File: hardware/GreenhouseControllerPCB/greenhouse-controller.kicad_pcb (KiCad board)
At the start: 2 copper layers, 208 x 132 mm, 72 parts, among them J1 Motor 2, J10 ALARM contact, J11 AC-Mains, J12 DM1AA-SF-PEJ72, J13 MODBUS RS485 S200, J2 24V in, J3 I2C Display, J4 Keypad, J6 Motor 3, J7 Motor 1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

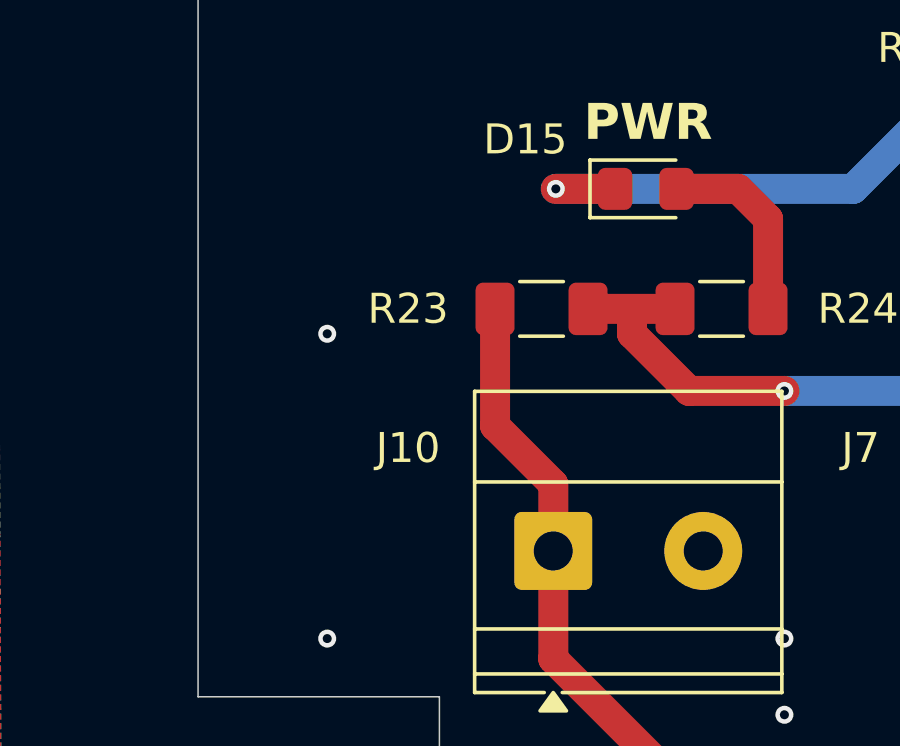
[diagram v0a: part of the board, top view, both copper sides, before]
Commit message: rc.1.5.5 — IO MUX pin glitch filter on GPIO42 (motor-alarm EMI defense)
Software complement to the 1.8 kΩ shunt resistor installed on unit
5C88 (2026-05-29) across the alarm input pad. The shunt sets a
current-amplitude floor that EMI must overcome to flip the GPIO
through threshold (lowering source impedance from 1 kΩ to ~643 Ω);
this filter sets a duration floor at the IO MUX (~25 ns) before any
interrupt is raised.

ESP-IDF's gpio_new_pin_glitch_filter() inserts a 2-IO-MUX-clock-cycle
filter into the input path between the pad and the GPIO matrix
interrupt logic. Sub-25 ns pulses — the bulk of capacitively-coupled
EMI on long unterminated cables — are dropped at silicon, costing
zero CPU cycles. Genuine mechanical alarm-contact transitions settle
in ≥ 1 ms so they pass through unaffected.

The four-layer defense stack now in place on the alarm pipeline:

  hardware divider  → amplitude floor (~mA injection required)   [HW]
  pin glitch filter → duration floor (≥ 25 ns to register)       [rc.1.5.5]
  ISR rate-limit    → ≥ 5 ms between accepted edges              [rc.1.5.3]
  task debounce     → re-read live pin 75 ms after edge          [rc.1.4 baseline]

For an EMI event to now produce a spurious alarm it must clear all
four floors simultaneously. Real alarm transitions clear them by
construction.

Failure to create the filter is non-fatal — the rate-limit + task
debounce remain in place, just less robustly; a warning is logged
and operation continues. On success: ESP_LOGI emits
"GPIO42 pin glitch filter enabled (~25 ns IO MUX drop)" at boot.

Build + OTA verified on unit 5C88 (192.168.20.150):
  fw_ver         = 2.0.0-rc.1.5.5
  asset_version  = 2.0.0-rc.1.5.5
  bank=A accepted=true (past T1's 30 s healthy mark)
  no rollback, no coredump

Flash: 64.7 % → 64.8 % (+1504 B — IDF gpio_filter component).
RAM:   18.9 % unchanged (+8 B handle pointer in .bss).

Added pull down resistor to PCB for alarm input tom meet 3,3V compliance of GPIO and mitigate EMI on input.
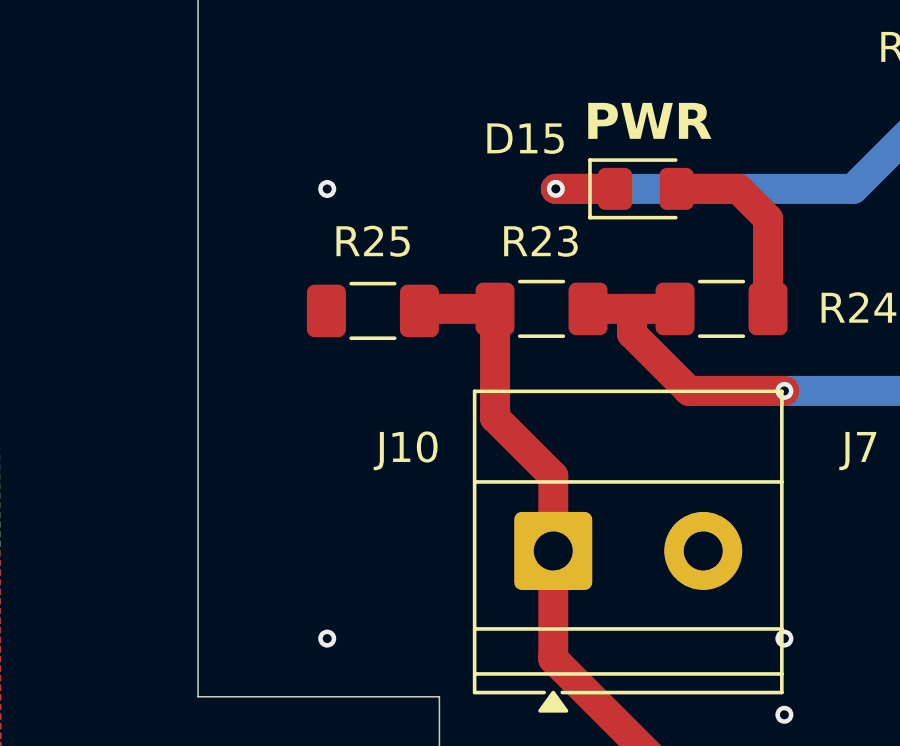
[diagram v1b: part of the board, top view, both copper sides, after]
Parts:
- added R25: 1K8, Resistor_SMD:R_1206_3216Metric_Pad1.30x1.75mm_HandSolder, F.Cu at (49.8, 126.2)
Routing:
- net /OPTO_INPUT: track 213.4 -> 216.0 mm
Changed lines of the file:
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@@
 	(title_block
 		(title "PCB Kas-controller Wenumseveld")
-		(date "2026-05-01")
+		(date "2026-05-29")
 		(rev "Remko Welling")
 		(company "RFSee")
 		(comment 1 "remko@rfsee.nl")
 		(comment 2 "https://www.rfsee.nl")
-		(comment 3 "V 1.1.0")
+		(comment 3 "V 1.1.1")
 	)
 	(layers
@@
 		)
 	)
+	(footprint "Resistor_SMD:R_1206_3216Metric_Pad1.30x1.75mm_HandSolder"
+		(layer "F.Cu")
+		(at 49.784 126.238 180)
+		(descr "Resistor SMD 1206 (3216 Metric), square (rectangular) end terminal, IPC-7351 nominal with elongated pad for handsoldering. (Body size source: IPC-SM-782 page 72, https://www.pcb-3d.com/wordpress/wp-content/uploads/ipc-sm-782a_amendment_1_and_2.pdf)")
+		(tags "resistor handsolder")
+		(property "Reference" "R25"
+			(at 0 2.286 0)
+			(layer "F.SilkS")
+			(effects
+				(font
+					(size 1 1)
+					(thickness 0.15)
+				)
+			)
+		)
+		(property "Value" "1K8"
+			(at 0 1.83 0)
+			(layer "F.Fab")
+			(effects
+				(font
+					(size 1 1)
+					(thickness 0.15)
+				)
+			)
+		)
+		(property "Datasheet" ""
+			(at 0 0 0)
+			(layer "F.Fab")
+			(hide yes)
+			(effects
+				(font
+					(size 1.27 1.27)
+				)
+			)
+		)
+		(property "Description" "Resistor"
+			(at 0 0 0)
+			(layer "F.Fab")
+			(hide yes)
+			(effects
+				(font
+					(size 1.27 1.27)
+				)
+			)
+		)
+		(property ki_fp_filters "R_*")
+		(sheetname "/")
+		(sheetfile "greenhouse-controller.kicad_sch")
+		(units
+			(unit
+				(name "A")
+				(pins "1" "2")
+			)
+		)
+		(attr smd)
+		(duplicate_pad_numbers_are_jumpers no)
+		(fp_line
+			(start -0.727064 0.91)
+			(end 0.727064 0.91)
+			(stroke
+				(width 0.12)
+				(type solid)
+			)
+			(layer "F.SilkS")
+		)
+		(fp_line
+			(start -0.727064 -0.91)
+			(end 0.727064 -0.91)
+			(stroke
+				(width 0.12)
+				(type solid)
+			)
+			(layer "F.SilkS")
+		)
+		(fp_rect
+			(start -2.45 -1.13)
+			(end 2.45 1.13)
+			(stroke
+				(width 0.05)
+				(type solid)
+			)
+			(fill no)
+			(layer "F.CrtYd")
+		)
+		(fp_rect
+			(start -1.6 -0.8)
+			(end 1.6 0.8)
+			(stroke
+				(width 0.1)
+				(type solid)
+			)
+			(fill no)
+			(layer "F.Fab")
+		)
+		(fp_text user "${REFERENCE}"
+			(at 0 0 0)
+			(layer "F.Fab")
+			(effects
+				(font
+					(size 0.8 0.8)
+					(thickness 0.12)
+				)
+			)
+		)
+		(pad "1" smd roundrect
+			(at -1.55 0 180)
+			(size 1.3 1.75)
+			(layers "F.Cu" "F.Mask" "F.Paste")
+			(roundrect_rratio 0.192308)
+			(net "/OPTO_INPUT")
+			(pintype "passive")
+		)
+		(pad "2" smd roundrect
+			(at 1.55 0 180)
+			(size 1.3 1.75)
+			(layers "F.Cu" "F.Mask" "F.Paste")
+			(roundrect_rratio 0.192308)
+			(net "/GND")
+			(pintype "passive")
+		)
+		(embedded_fonts no)
+		(model "${KICAD10_3DMODEL_DIR}/Resistor_SMD.3dshapes/R_1206_3216Metric.step"
+			(offset
+				(xyz 0 0 0)
+			)
+			(scale
+				(xyz 1 1 1)
+			)
+			(rotate
+				(xyz 0 0 0)
+			)
+		)
+	)
 	(footprint "my-KiCad-library:SRD-05VDC-SL-C"
 		(layer "F.Cu")
@@
 		(tags "resistor handsolder")
 		(property "Reference" "R23"
-			(at 4.45 0 0)
+			(at 0.033 2.218 0)
 			(layer "F.SilkS")
 			(effects
@@
 	)
 	(via
-		(at 48.26 127)
+		(at 48.26 122.174)
 		(size 0.6)
 		(drill 0.3)
@@
 	)
 	(segment
-		(start 151.13 111.252)
-		(end 163.83 111.252)
+		(start 51.402 126.17)
+		(end 51.334 126.238)
 		(width 1)
 		(layer "F.Cu")
@@
 	)
 	(segment
-		(start 55.794286 134.239)
-		(end 55.794286 132.009286)
+		(start 55.794286 131.740286)
+		(end 53.848 129.794)
+		(width 1)
+		(layer "F.Cu")
+		(net "/OPTO_INPUT")
+	)
+	(segment
+		(start 151.13 111.252)
+		(end 163.83 111.252)
 		(width 1)
 		(layer "F.Cu")
@@
 	)
 	(segment
-		(start 179.07 59.182)
-		(end 177.038 57.15)
+		(start 53.855 126.17)
+		(end 51.402 126.17)
 		(width 1)
 		(layer "F.Cu")
@@
 	)
 	(segment
-		(start 53.855 130.07)
-		(end 53.855 126.17)
+		(start 179.07 59.182)
+		(end 177.038 57.15)
 		(width 1)
 		(layer "F.Cu")
@@
 	)
 	(segment
+		(start 53.848 129.794)
+		(end 53.855 129.787)
+		(width 1)
+		(layer "F.Cu")
+		(net "/OPTO_INPUT")
+	)
+	(segment
 		(start 55.794286 134.239)
 		(end 55.794286 137.836286)
@@
 	)
 	(segment
+		(start 53.855 129.787)
+		(end 53.855 126.17)
+		(width 1)
+		(layer "F.Cu")
+		(net "/OPTO_INPUT")
+	)
+	(segment
 		(start 163.83 111.252)
 		(end 179.07 96.012)
@@
 	)
 	(segment
-		(start 55.794286 137.836286)
-		(end 64.262 146.304)
+		(start 55.794286 134.239)
+		(end 55.794286 131.740286)
 		(width 1)
 		(layer "F.Cu")
@@
 	)
 	(segment
-		(start 179.07 96.012)
-		(end 179.07 59.182)
+		(start 55.794286 137.836286)
+		(end 64.262 146.304)
 		(width 1)
 		(layer "F.Cu")
@@
 	)
 	(segment
-		(start 55.794286 132.009286)
-		(end 53.855 130.07)
+		(start 179.07 96.012)
+		(end 179.07 59.182)
 		(width 1)
 		(layer "F.Cu")
